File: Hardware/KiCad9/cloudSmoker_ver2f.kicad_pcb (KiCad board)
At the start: 4 copper layers, 70 x 70 mm, 89 parts, among them J1 Conn_01x02_Pin, J11 Conn_01x04_Pin, J15 Conn_01x04_Pin, J3 Conn_01x04_Pin, J6 Conn_01x04_Pin, J7 Conn_01x05, Q1 BSS138, Q2 BSS138, SW2 SW_Push_Dual, SW3 SW_Push_Dual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

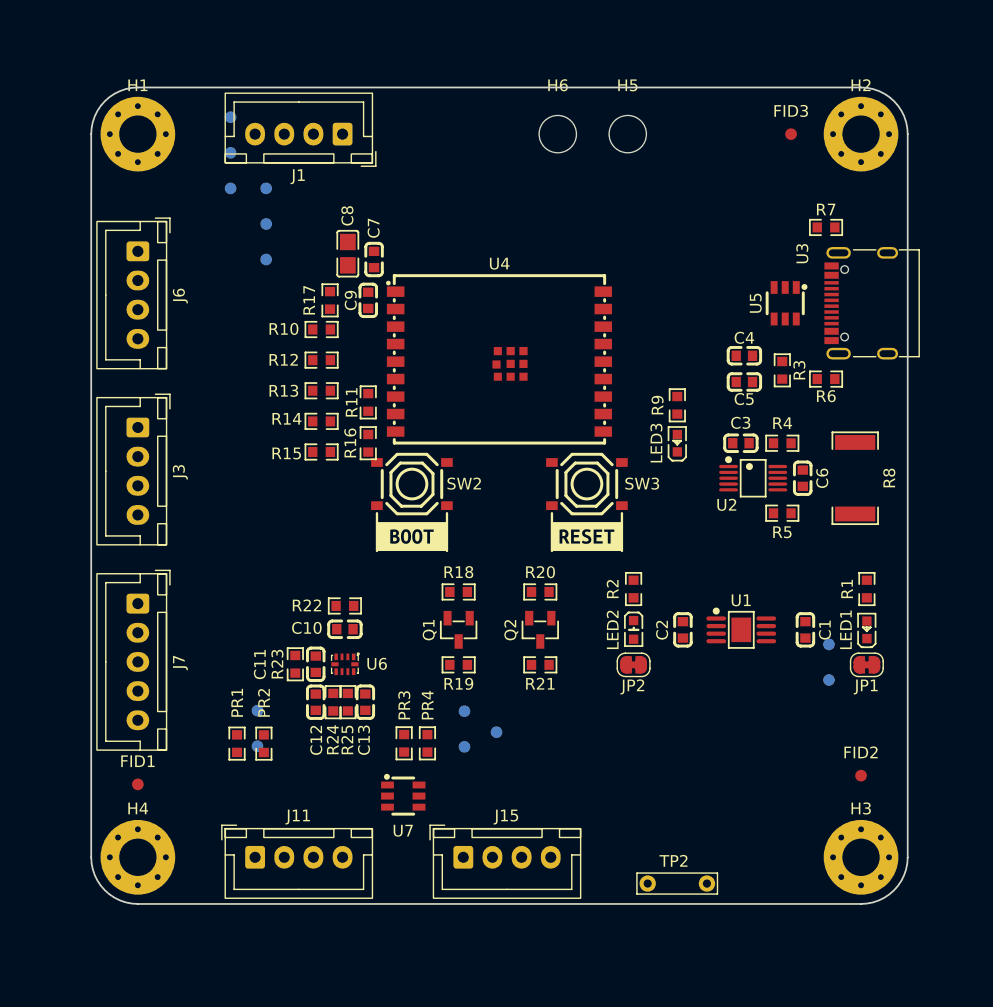
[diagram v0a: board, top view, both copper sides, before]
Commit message: update hardware version number to 2f
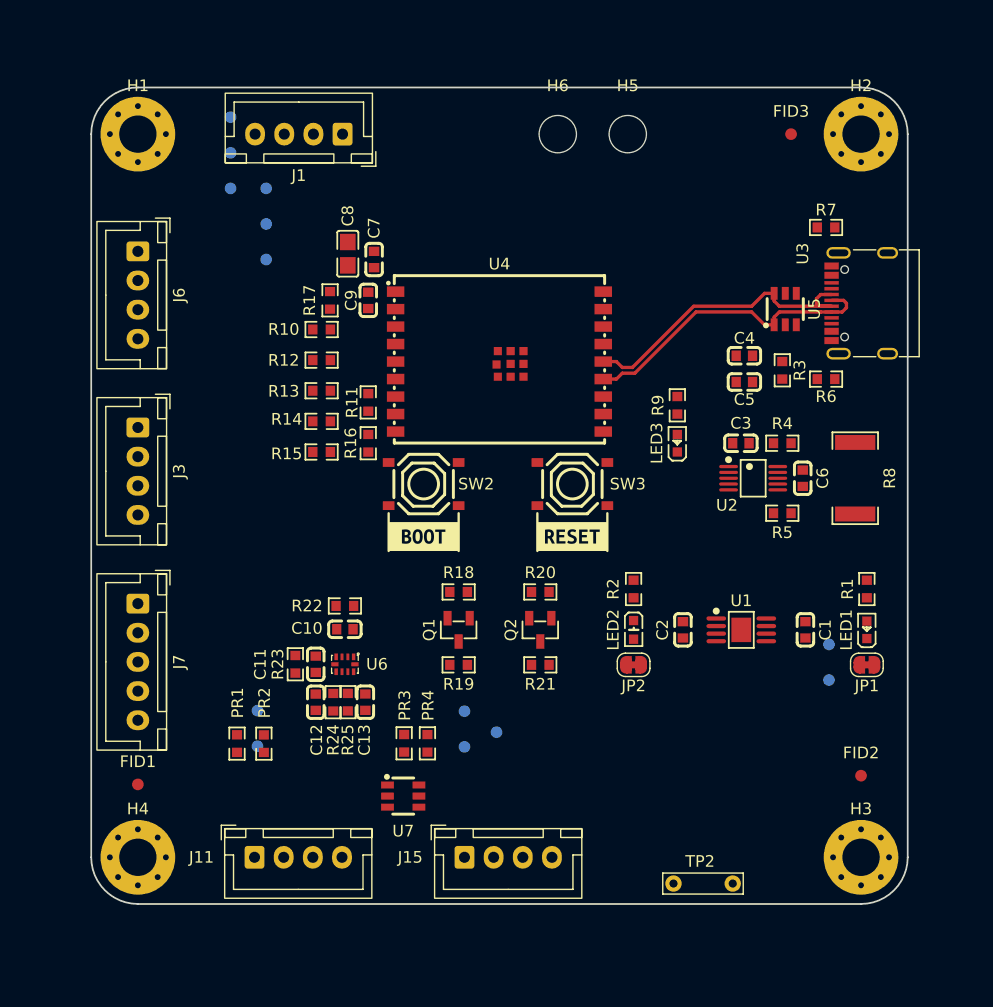
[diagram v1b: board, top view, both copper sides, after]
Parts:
- moved TP2 2.21 mm to (149.0, 128.2)
- moved SW3 1.25 mm to (135.2, 94.0)
- moved kibuzzard-6A0E9251 1.25 mm to (135.2, 98.5)
- moved SW2 1.00 mm to (122.5, 94.0)
- moved kibuzzard-6A0E9267 1.00 mm to (122.5, 98.5)
- moved U5 0.50 mm to (153.5, 79.0), turned to -90 degrees
- moved J15 0.10 mm to (126.0, 126.0)
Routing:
- net USB_D+: track 0.00 -> 26.4 mm
- net USB_D-: track 0.00 -> 26.4 mm

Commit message: Update cloudSmoker_ver2f
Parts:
- TP2: renamed from TP3; moved to F.Cu
- TP3: renamed from TP4; moved to F.Cu
- TP4: renamed from TP5; moved to F.Cu
- TP5: renamed from TP1; moved to F.Cu
- TP6, TP7, TP8, TP9: moved to F.Cu
- U4: footprint JLCImport:ESP32-C3-WROOM-02U-N4 -> RF_Module:ESP32-C3-WROOM-02U
- U6: value ADS1115IRUGR -> ~
- moved TP6 39.0 mm to (129.6, 93.6)
- moved TP8 28.4 mm to (110.5, 93.6)
- moved TP12 19.8 mm to (110.0, 109.0)
- moved TP13 16.9 mm to (110.0, 111.0)
- moved PR1 15.1 mm to (113.8, 103.0), turned to 180 degrees
- moved TP14 14.6 mm to (111.8, 109.8)
- moved TP3 12.7 mm to (121.4, 74.6)
- moved TP4 11.7 mm to (120.1, 72.4)
- moved TP7 10.5 mm to (104.2, 79.0)
- moved TP10 9.39 mm to (111.8, 107.8)
- moved TP5 8.00 mm to (158.1, 102.8)
- moved PR3 7.08 mm to (113.8, 116.3), turned to 180 degrees
- moved Q2 7.00 mm to (125.5, 106.5)
- moved R20 7.00 mm to (125.5, 103.2)
- moved R21 7.00 mm to (125.5, 109.5)
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- renumbered R6 to R5, R5 to R6, TP2 to TP1
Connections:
- C5 pad 1: VBUS -> VBUSF
- C6 pad 1: VBUS -> /Load
- C6 pad 2: +5V -> /Supply
- J7 pad 2: ENC_CLK -> ENC_DT
- J7 pad 3: ENC_DT -> ENC_CLK
- R11 pad 2: DISP_CS -> Net-(U4-IO8)
- R14 pad 2: DISP_CS -> Net-(U4-IO8)
- R3 pad 2: VBUS -> VBUSF
- R4 pad 1: VBUS -> /Supply
- R4 pad 2: /Supply -> VBUSF
- R6 pad 1: +5V -> /Load
- R6 pad 2: /Load -> +5V
- R8 pad 1: VBUS -> VBUSF
- U2 pad 8: +5V -> /Load
- U4 pad 7: DISP_CS -> Net-(U4-IO8)
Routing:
- net GND: track 0.00 -> 81.5 mm, vias 0 -> 52
- net ENC_DT: track 0.00 -> 55.9 mm, vias 0 -> 1
- net ENC_CLK: track 0.00 -> 55.9 mm, vias 0 -> 1
- net ENC_SW: track 0.00 -> 53.6 mm, vias 0 -> 1
- net I2C_SDA_3V3: track 0.00 -> 52.3 mm, vias 0 -> 2
- net I2C_SCL_3V3: track 0.00 -> 51.0 mm, vias 0 -> 2
- net /PIT_IN: track 0.00 -> 48.0 mm
- net DEBUG_TX/LED: track 0.00 -> 45.0 mm
- net DEBUG_RX: track 0.00 -> 42.4 mm
- net ~{BOOT}_DISP_RST: track 0.00 -> 34.6 mm
- net ~{RESET}: track 0.00 -> 34.4 mm
- net /MEAT1_IN: track 0.00 -> 31.2 mm
- net DISP_BL: track 0.00 -> 28.5 mm, vias 0 -> 1
- net /MEAT2_IN: track 0.00 -> 25.2 mm
- net /MEAT3_IN: track 0.00 -> 24.5 mm
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- added copper zone on F.Cu, net +3.3V
- added copper zone on In2.Cu, net +3.3V
- added copper zone on F.Cu, net +5V
- added copper zone on In2.Cu, net +5V
- added copper zone on B.Cu, net GND
- added copper zone on F.Cu, net GND
- added copper zone on In1.Cu, net GND
- added copper zone on F.Cu, net VBUS
- added copper zone on F.Cu, net VBUSF

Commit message: update hardware files for v2f
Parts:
- added QR*****: QR-Code_cloudSmoker_Github_wiki, JLCImport:QR-Code_cloudSmoker_Github_wiki, F.Cu at (149.4, 116.1)
- added REF**: Logo_cloudSmoker2, JLCImport:Logo_cloudSmoker2, F.Cu at (156.0, 124.4)
- added REF**: OSHW-Logo2_7.3x6mm_SilkScreen, Symbol:OSHW-Logo2_7.3x6mm_SilkScreen, B.Cu at (141.2, 71.5)
- added REF**: KiCad-Logo2_5mm_SilkScreen, Symbol:KiCad-Logo2_5mm_SilkScreen, B.Cu at (149.0, 88.4)
- added kibuzzard-6A1EB0C4: G***, kibuzzard-6A1EB0C4, F.Cu at (102.0, 68.8)
- added kibuzzard-6A1FD9A8: G***, kibuzzard-6A1FD9A8, F.Cu at (138.0, 67.6)
- added kibuzzard-6A24E1FA: G***, kibuzzard-6A24E1FA, F.Cu at (149.4, 123.1)
- J11, J15: footprint Connector_JST:JST_XH_B4B-XH-A_1x04_P2.50mm_Vertical -> JLCImport:JST_XH_B4B-XH-A_1x04_P2.50mm_Vertical_two_gnd
- TP1 - GND: renamed from TP1
- TP2 GND: renamed from TP2
- TP5 +5V: renamed from TP5
- U3: footprint Connector_USB:USB_C_Receptacle_G-Switch_GT-USB-7010ASV -> JLCImport:USB_C_Receptacle_G-Switch_GT-USB-7010ASV
- U6: value ~ -> ADS1115IRUGR
- moved FID2 1.50 mm to (160.0, 120.5)
- moved FID1 0.75 mm to (98.0, 120.5)
- moved TP1 - GND 0.20 mm to (149.0, 128.1)
- moved TP13 0.18 mm to (110.0, 111.2)
- moved PR2 0.15 mm to (107.4, 109.5)
- moved C5 0.10 mm to (150.6, 85.2)
- moved R23 0.10 mm to (109.2, 109.5)
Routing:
- net GND: track 81.5 -> 83.7 mm, vias 52 -> 130
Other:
- board text added: "cloudSmoker2 Ver2f cwg Jun26"

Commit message: hardware updates
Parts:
- removed the REF** at (156.0, 124.4)
- removed kibuzzard-6A1FD9A8: G***, kibuzzard-6A1FD9A8
- removed kibuzzard-6A24E1FA: G***, kibuzzard-6A24E1FA
- added G***: LOGO, JLCImport:cloudSmoker icon 7mm, F.Cu at (147.9, 68.8)
- added G***: LOGO, JLCImport:cc licence logo, B.Cu at (143.8, 75.2)
- added REF**: cloudSmoker2 logo Lg h=25mm, JLCImport:cloudSmoker2 logo Lg h=25mm, F.Cu at (132.7, 120.1)
- added kibuzzard-6A262764: G***, kibuzzard-6A262764, F.Cu at (105.1, 109.3)
- added kibuzzard-6A262764: G***, kibuzzard-6A262764, B.Cu at (103.7, 109.0)
- added kibuzzard-6A265CBA: G***, kibuzzard-6A265CBA, F.Cu at (108.8, 121.8)
- added kibuzzard-6A265CBA: G***, kibuzzard-6A265CBA, B.Cu at (108.9, 122.2)
- added kibuzzard-6A265DB6: G***, kibuzzard-6A265DB6, F.Cu at (114.2, 121.8)
- added kibuzzard-6A265DB6: G***, kibuzzard-6A265DB6, B.Cu at (114.3, 122.1)
- added kibuzzard-6A265E44: G***, kibuzzard-6A265E44, F.Cu at (127.2, 121.8)
- added kibuzzard-6A265E44: G***, kibuzzard-6A265E44, B.Cu at (127.2, 122.2)
- added kibuzzard-6A265EBE: G***, kibuzzard-6A265EBE, F.Cu at (132.3, 121.8)
- added kibuzzard-6A265EBE: G***, kibuzzard-6A265EBE, B.Cu at (132.3, 122.2)
- added kibuzzard-6A2660A1: G***, kibuzzard-6A2660A1, F.Cu at (111.8, 69.7)
- added kibuzzard-6A2660A1: G***, kibuzzard-6A2660A1, B.Cu at (111.8, 68.0)
- added kibuzzard-6A266895: G***, kibuzzard-6A266895, F.Cu at (135.3, 67.9)
- added kibuzzard-6A266895: G***, kibuzzard-6A266895, B.Cu at (135.3, 67.9)
- added kibuzzard-6A266C13: G***, kibuzzard-6A266C13, F.Cu at (150.2, 123.6)
- added kibuzzard-6A276479: G***, kibuzzard-6A276479, F.Cu at (150.2, 110.3)
- added kibuzzard-6A28B67F: G***, kibuzzard-6A28B67F, F.Cu at (105.1, 85.3)
- added kibuzzard-6A28B67F: G***, kibuzzard-6A28B67F, B.Cu at (103.7, 85.4)
- TP1: renamed from TP1 - GND
- TP2: renamed from TP2 GND
- TP5: renamed from TP5 +5V
- U3: footprint JLCImport:USB_C_Receptacle_G-Switch_GT-USB-7010ASV -> JLCImport:USB_C_Receptacle_G-Switch_GT-USB-7010ASV clipped
- moved REF** 29.0 mm to (154.5, 116.9)
- moved REF** 10.4 mm to (131.6, 75.3)
- moved TP9 5.26 mm to (108.9, 78.9)
- moved TP7 3.58 mm to (107.3, 80.8)
- moved H5 2.10 mm to (138.8, 64.0)
- moved H6 2.10 mm to (131.9, 64.0)
- moved QR***** 1.45 mm to (150.2, 117.3)
- moved C4 1.40 mm to (150.6, 84.7)
- moved C5 1.40 mm to (150.6, 86.5)
- moved R3 1.40 mm to (153.2, 85.6)
- moved C3 0.94 mm to (151.4, 96.8), turned to 0 degrees
- moved kibuzzard-6A1EB0C4 0.88 mm to (102.8, 68.4)
- moved TP6 0.59 mm to (129.0, 93.7)
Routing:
- net GND: track 83.7 -> 85.5 mm, vias 130 -> 157
- net /MEAT3_IN: track 24.5 -> 23.5 mm
- net ~{RESET}: track 34.4 -> 35.1 mm
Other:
- board text added: "+3V3"
- board text added: "+5V"
- board text added: "3V3"
- board text added: "5V"
- board text added: "BL"
- board text added: "CLK"
- board text added: "CS"
- board text added: "DC"
- board text added: "DT"
- board text added: "Designed for use with R25=1MΩ thermistors only"
- board text added: "EN"
- board text added: "GND"
- board text added: "GND CLIP"
- board text added: "MEAT1"
- board text added: "MEAT2"
- board text added: "MEAT3"
- board text added: "MOSI"
- board text added: "PIT"
- board text added: "RST"
- board text added: "RX"
- board text added: "SCK"
- board text added: "SW"
- board text added: "TX"
- board text added: "cloudSmoker2 Ver2f cwg 9Jun26"
- board text removed: "cloudSmoker2 Ver2f cwg Jun26"

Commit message: update hardware files for cloudSmoker_ver2f
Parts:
- added kibuzzard-6A1EB0C4: G***, kibuzzard-6A1EB0C4, B.Cu at (156.0, 69.1)
- C9: footprint JLCImport:CC0603KRX7R9BB104 -> JLCImport:CL10A105KB8NNNC
- R10, R12, R13, R14, R15: footprint JLCImport:PTFR0603B120KP9 -> JLCImport:R0603_part-C23345
- R3: footprint JLCImport:PTFR0603B120KP9 -> JLCImport:R0603_part-C21189_0-ohm
- R4, R6: footprint JLCImport:PTFR0603B120KP9 -> JLCImport:R0603_part-C22859_10-ohm
- moved C5 0.22 mm to (150.5, 86.8)
- moved R12 0.12 mm to (113.8, 83.2)
- moved R14 0.12 mm to (113.8, 88.5)
- moved C3 0.11 mm to (151.5, 96.8)
- moved C4 0.11 mm to (150.5, 84.8)
- moved C6 0.10 mm to (153.5, 93.5)
- moved PR2 0.10 mm to (107.5, 109.5)
- moved PR3 0.10 mm to (113.8, 116.2)
- moved PR4 0.10 mm to (117.2, 116.2)
- moved R3 0.10 mm to (153.2, 85.5)
- turned R4 to 180 degrees
- turned R6 to 180 degrees
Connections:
- R4 pad 1: /Supply -> VBUSF
- R4 pad 2: VBUSF -> /Supply
- R6 pad 1: /Load -> +5V
- R6 pad 2: +5V -> /Load

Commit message: updated:   Hardware/KiCad9/cloudSmoker_ver2f.kicad_pcb
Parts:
- moved FID3 31.5 mm to (122.5, 64.0)
- moved FID2 2.97 mm to (160.0, 117.5)
- moved FID1 1.75 mm to (98.0, 118.8)
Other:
- board text added: "cloudSmoker2 Ver2f cwg 16Jun26"
- board text removed: "cloudSmoker2 Ver2f cwg 9Jun26"
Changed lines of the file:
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@@
 		(aux_axis_origin 94 130)
 		(pcbplotparams
-			(layerselection 0x00000000_00000000_55555555_5755f5ff)
-			(plot_on_all_layers_selection 0x00000000_00000000_00000000_00000000)
+			(layerselection 0x00000000_00000000_55555555_55555501)
+			(plot_on_all_layers_selection 0x00000000_00000000_00000000_02000000)
 			(disableapertmacros no)
 			(usegerberextensions no)
@@
 			(psnegative no)
 			(psa4output no)
-			(plot_black_and_white yes)
+			(plot_black_and_white no)
 			(sketchpadsonfab no)
 			(plotpadnumbers no)
@@
 			(crossoutdnponfab yes)
 			(subtractmaskfromsilk no)
-			(outputformat 1)
+			(outputformat 5)
 			(mirror no)
-			(drillshape 1)
+			(drillshape 0)
 			(scaleselection 1)
-			(outputdirectory "")
+			(outputdirectory "svg_files/")
 		)
 	)
@@
 	(footprint "Fiducial:Fiducial_1mm_Mask2mm"
 		(layer "F.Cu")
-		(at 154 64)
+		(at 122.525 64)
 		(descr "Fiducial, circular marking, 1mm bare copper, 2mm soldermask opening (Level A)")
 		(tags "fiducial")
 		(property "Reference" "FID3"
-			(at 0 -1.9 0)
+			(at -0.025 2.05 0)
 			(layer "F.SilkS")
 			(effects
@@
 		)
 		(property "Value" "Fiducial"
-			(at 0 1.95 0)
+			(at 0 -1.9 0)
 			(layer "F.Fab")
 			(effects
@@
 		(sheetname "/")
 		(sheetfile "cloudSmoker_ver2f.kicad_sch")
-		(attr smd exclude_from_bom)
+		(attr smd exclude_from_pos_files exclude_from_bom)
 		(fp_circle
 			(center 0 0)
@@
 	(footprint "Fiducial:Fiducial_1mm_Mask2mm"
 		(layer "F.Cu")
-		(at 98 120.5)
+		(at 98 118.75)
 		(descr "Fiducial, circular marking, 1mm bare copper, 2mm soldermask opening (Level A)")
 		(tags "fiducial")
 		(property "Reference" "FID1"
-			(at 0 -1.9 0)
+			(at -0.05 2.1 0)
 			(layer "F.SilkS")
 			(effects
@@
 		)
 		(property "Value" "Fiducial"
-			(at 0 1.95 0)
+			(at -0.025 -1.95 0)
 			(layer "F.Fab")
 			(effects
@@
 		(sheetname "/")
 		(sheetfile "cloudSmoker_ver2f.kicad_sch")
-		(attr smd exclude_from_bom)
+		(attr smd exclude_from_pos_files exclude_from_bom)
 		(fp_circle
 			(center 0 0)
@@
 	(footprint "Fiducial:Fiducial_1mm_Mask2mm"
 		(layer "F.Cu")
-		(at 160 120.5)
+		(at 160 117.525)
 		(descr "Fiducial, circular marking, 1mm bare copper, 2mm soldermask opening (Level A)")
 		(tags "fiducial")
@@
 		(sheetname "/")
 		(sheetfile "cloudSmoker_ver2f.kicad_sch")
-		(attr smd exclude_from_bom)
+		(attr smd exclude_from_pos_files exclude_from_bom)
 		(fp_circle
 			(center 0 0)
@@
 		(tags "connector JST XH vertical")
 		(property "Reference" "J1"
-			(at -4.975 0.1 0)
+			(at 11.575 0.125 0)
 			(layer "F.SilkS")
 			(effects
@@
 		)
 	)
-	(gr_text "cloudSmoker2 Ver2f\ncwg 9Jun26"
+	(gr_text "cloudSmoker2 Ver2f\ncwg 16Jun26"
 		(at 119.97 77.96 0)
 		(layer "B.SilkS")
